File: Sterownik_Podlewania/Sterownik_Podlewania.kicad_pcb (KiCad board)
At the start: 2 copper layers, 89 parts, among them J1 Conn_01x06_Socket, J10 Screw_Terminal_01x02, J11 Screw_Terminal_01x02, J12 Screw_Terminal_01x02, J13 Screw_Terminal_01x02, J14 Screw_Terminal_01x02, J15 Screw_Terminal_01x02, J16 Screw_Terminal_01x02, J2 Conn_01x06_Socket, J3 RJ45, J4 Conn_01x04_Socket, J5 RJ45, J6 RJ45, J7 Conn_01x05_Socket, J8 RJ45, J9 Screw_Terminal_01x02, K1 SANYOU_SRD_Form_C, K2 SANYOU_SRD_Form_C, K3 SANYOU_SRD_Form_C, K4 SANYOU_SRD_Form_C, K5 SANYOU_SRD_Form_C, Q1 BC547, Q2 BC547, Q3 BC547, Q4 BC547, Q5 BC547, SW1 SW_Nidec_CAS-120A1, SW2 SW_Nidec_CAS-120A1, SW3 SW_Nidec_CAS-120A1, SW4 SW_Nidec_CAS-120A1, SW5 SW_Nidec_CAS-120A1, SW6 SW_Nidec_CAS-120A1, SW8 SW_Nidec_CAS-120A1, U1 ESP32-DEVKITC, U2 HHG1D-1, U3 L7805

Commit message: Dodanie footprintów schotky, kondesatorów
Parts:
- added C10: 0.1u, Capacitor_THT:C_Disc_D3.0mm_W1.6mm_P2.50mm, F.Cu at (487.2, 88.5)
- added C7: 0.33u, Capacitor_THT:CP_Axial_L10.0mm_D4.5mm_P15.00mm_Horizontal, F.Cu at (453.0, 86.7)
- added C8: 0.1u, Capacitor_THT:C_Disc_D3.0mm_W1.6mm_P2.50mm, F.Cu at (483.8, 75.0)
- added C9: 0.1u, Capacitor_THT:C_Disc_D3.0mm_W1.6mm_P2.50mm, F.Cu at (482.8, 81.5)
- added D19: D_Schottky, Diode_SMD:D_SOD-123, F.Cu at (-149.8, -12.7)
- added D20: D_Schottky, Diode_SMD:D_SOD-123, F.Cu at (-149.8, -9.34)
- added D21: D_Schottky, Diode_SMD:D_SOD-123, F.Cu at (-149.8, -3.99)
- added U4: LD1117S33TR_SOT223, Package_TO_SOT_SMD:SOT-223-3_TabPin2, F.Cu at (4.42, 3.70)
- J4: footprint Connector_Harwin:Harwin_M20-89006xx_1x06_P2.54mm_Horizontal -> Connector_Harwin:Harwin_M20-89004xx_1x04_P2.54mm_Horizontal

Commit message: Dodanie modeli 3d, nowy footprint do przełącznika, przerzucenie na drugą stronę płytki elementów, wstępne rozdzielenie elemntów pasywnych
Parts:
- C1, C11, C2, C3, C4, C5, C6, R11, R12, R14, R16, R18, R20, R21, R22, R23, R24, R25, R26, R27, R28, R3, R6, R7, R8, R9: moved to B.Cu
- J1, J2: footprint Connector_Harwin:Harwin_M20-89006xx_1x06_P2.54mm_Horizontal -> Connector_PinHeader_2.54mm:PinHeader_1x06_P2.54mm_Vertical
- J4: footprint Connector_Harwin:Harwin_M20-89004xx_1x04_P2.54mm_Horizontal -> Connector_PinHeader_2.54mm:PinHeader_1x04_P2.54mm_Vertical
- J7: footprint Connector_Harwin:Harwin_M20-89005xx_1x05_P2.54mm_Horizontal -> Connector_PinHeader_2.54mm:PinHeader_1x05_P2.54mm_Vertical
- SW1, SW2, SW3, SW4, SW5, SW6, SW8: footprint Button_Switch_SMD:Nidec_Copal_CAS-120A -> Toggle_Switch:Toggle Switch Bootland 4.7mm
- U1: footprint RF_Module:ESP32-C3-DevKitM-1 -> ESP32:MODULE_ESP32-DEVKITC
- U2: footprint Relay_THT:Relay_NCR_HHG1D-1 -> Relay_THT:RELAY_G3MB-202P
- U4: footprint Package_TO_SOT_SMD:SOT-223-3_TabPin2 -> Package_TO_SOT_THT:TO-220-3_Vertical
- moved C3 469.6 mm to (63.8, 157.7), turned to 90 degrees
- moved R24 464.2 mm to (70.3, 165.6), turned to 180 degrees
- moved R14 452.2 mm to (70.0, 144.8), turned to 180 degrees
- moved R17 434.7 mm to (86.6, 116.8)
- moved C2 434.1 mm to (97.8, 156.4), turned to 90 degrees
- moved R19 433.0 mm to (79.4, 116.6)
- moved R13 431.8 mm to (84.0, 121.9)
- moved R23 425.5 mm to (105.3, 167.1), turned to 180 degrees
- moved C11 424.7 mm to (113.3, 157.5), turned to 90 degrees
- moved C4 422.3 mm to (88.2, 151.1), turned to 180 degrees
- moved R16 420.4 mm to (85.5, 141.0), turned to 180 degrees
- moved R15 420.4 mm to (90.1, 122.2)
- moved R28 420.2 mm to (119.3, 165.6), turned to 180 degrees
- moved R25 417.2 mm to (92.6, 147.8), turned to 180 degrees
- moved D12 416.4 mm to (75.8, 69.3)
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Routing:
- net (no net): vias 0 -> 6

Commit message: dodanie modeli 3d, poprawa footprintu RTC
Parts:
- removed J2: Conn_01x06_Socket, Connector_PinHeader_2.54mm:PinHeader_1x06_P2.54mm_Vertical
- removed J7: Conn_01x05_Socket, Connector_PinHeader_2.54mm:PinHeader_1x05_P2.54mm_Vertical
- added J18: RJ45, Connector_RJ:RJ45_Amphenol_54602-x08_Horizontal, F.Cu at (41.9, 71.1)
- added R29: R, Resistor_SMD:R_1206_3216Metric, B.Cu at (153.9, 76.2)
- added R30: R, Resistor_SMD:R_1206_3216Metric, B.Cu at (153.9, 79.5)
- added U5: 757, Voltage_Level_Converters:MODULE_757, F.Cu at (81.3, 113.0)
- added U6: ~, RTC:RTC DS1307 + 32kb EEPROM 24C32 I2C, F.Cu at (113.7, 115.6)
- C7: footprint Capacitor_THT:CP_Axial_L10.0mm_D4.5mm_P15.00mm_Horizontal -> Capacitor_SMD:CP_Elec_4x5.4
- D10, D14, D16, D8, R1, R10, R13, R15, R17, R19, R2, R4, R5: moved to B.Cu
- J1: value Conn_01x06_Socket -> Barrel_Jack_MountingPin; footprint Connector_PinHeader_2.54mm:PinHeader_1x06_P2.54mm_Vertical -> Connector_BarrelJack:BarrelJack_GCT_DCJ200-10-A_Horizontal
- moved R22 115.1 mm to (77.2, 122.4)
- moved R3 115.1 mm to (82.3, 98.2)
- moved R6 115.1 mm to (82.9, 103.1)
- moved R7 115.1 mm to (101.4, 111.5)
- moved R8 115.1 mm to (102.8, 119.6)
- moved R9 115.1 mm to (92.4, 127.5)
- moved C8 113.6 mm to (66.0, 96.5)
- moved C9 102.5 mm to (76.2, 96.5)
- moved C10 102.4 mm to (86.4, 96.5)
- moved D21 98.0 mm to (98.2, 96.5)
- moved C7 97.2 mm to (58.5, 81.5), turned to 0 degrees
- moved R15 97.0 mm to (45.4, 36.1), turned to 180 degrees
- moved R10 96.0 mm to (46.6, 24.9), turned to 180 degrees
- moved R17 94.0 mm to (49.0, 30.7), turned to 180 degrees
- moved J1 92.6 mm to (43.5, 56.2), turned to -90 degrees
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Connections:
- J1 pad 1: SDA -> VP
- J1 pad 2: SCL -> GND
- U1 pad 4: unconnected-(U1-SENSOR_VN-Pad4) -> /Czujnik ciśnienia output
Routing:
- net (no net): vias 6 -> 3

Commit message: Wstępny finalny rozkład płytki, narysowanie outlinu
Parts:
- added REF**: MountingHole_3.2mm_M3_Pad_Via, MountingHole:MountingHole_3.2mm_M3_Pad_Via, F.Cu at (197.5, 150.0)
- added REF**: MountingHole_3.2mm_M3_Pad_Via, MountingHole:MountingHole_3.2mm_M3_Pad_Via, F.Cu at (42.5, 40.0)
- added REF**: MountingHole_3.2mm_M3_Pad_Via, MountingHole:MountingHole_3.2mm_M3_Pad_Via, F.Cu at (42.5, 150.0)
- added REF**: MountingHole_3.2mm_M3_Pad_Via, MountingHole:MountingHole_3.2mm_M3_Pad_Via, F.Cu at (197.5, 40.0)
- D12: moved to B.Cu
- R1, R2: moved to F.Cu
- U4: footprint Package_TO_SOT_THT:TO-220-3_Vertical -> Package_TO_SOT_SMD:SOT-223
- moved R5 166.1 mm to (193.5, 97.5)
- moved R4 164.3 mm to (193.2, 89.8)
- moved R2 143.9 mm to (152.5, 105.0), turned to 0 degrees
- moved J1 139.9 mm to (183.2, 48.6), turned to 180 degrees
- moved R1 135.8 mm to (152.5, 100.5)
- moved C7 129.0 mm to (187.5, 79.3), turned to 90 degrees
- moved R10 113.1 mm to (118.4, 112.2), turned to 90 degrees
- moved C8 112.2 mm to (174.2, 67.0)
- moved R22 106.6 mm to (182.7, 137.2)
- moved D2 103.8 mm to (193.9, 95.0)
- moved R3 100.7 mm to (182.6, 89.7)
- moved R6 99.8 mm to (182.6, 99.7)
- moved R19 99.2 mm to (129.1, 97.7), turned to 90 degrees
- moved J8 98.9 mm to (49.0, 51.0)
- moved C9 97.6 mm to (167.0, 60.8), turned to -90 degrees
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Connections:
- U1 pad 15: /WIFI -> /SEN0193_WYJŚCIE
- U1 pad 23: /SEN0193_WYJŚCIE -> /TRYB
- U1 pad 24: /TRYB -> /WIFI
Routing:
- net (no net): track 0.00 -> 160.0 mm
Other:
- board outline added: 165 x 120 mm

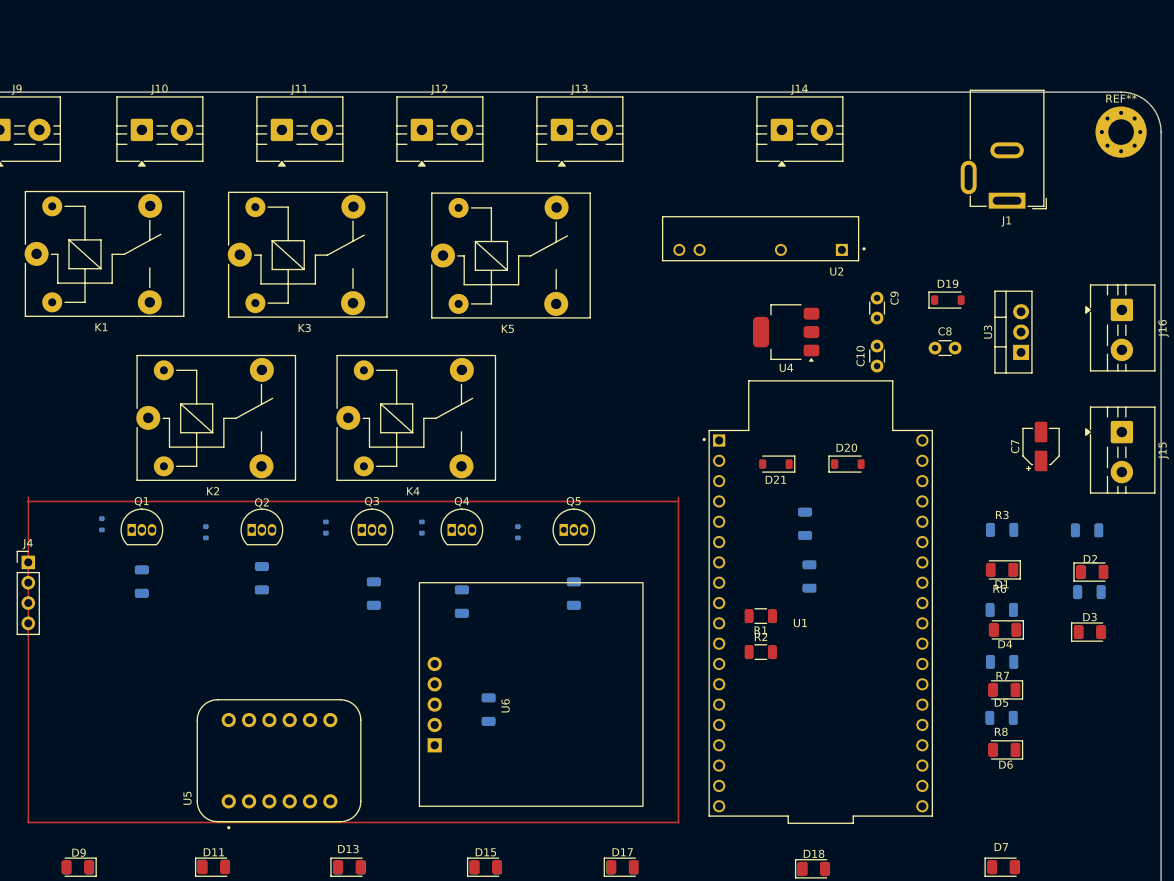
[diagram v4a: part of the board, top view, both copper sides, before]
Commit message: Zmiana footprintó diód przekaźnika na schottky,finalne ułożenie  przekaźników, diód itp
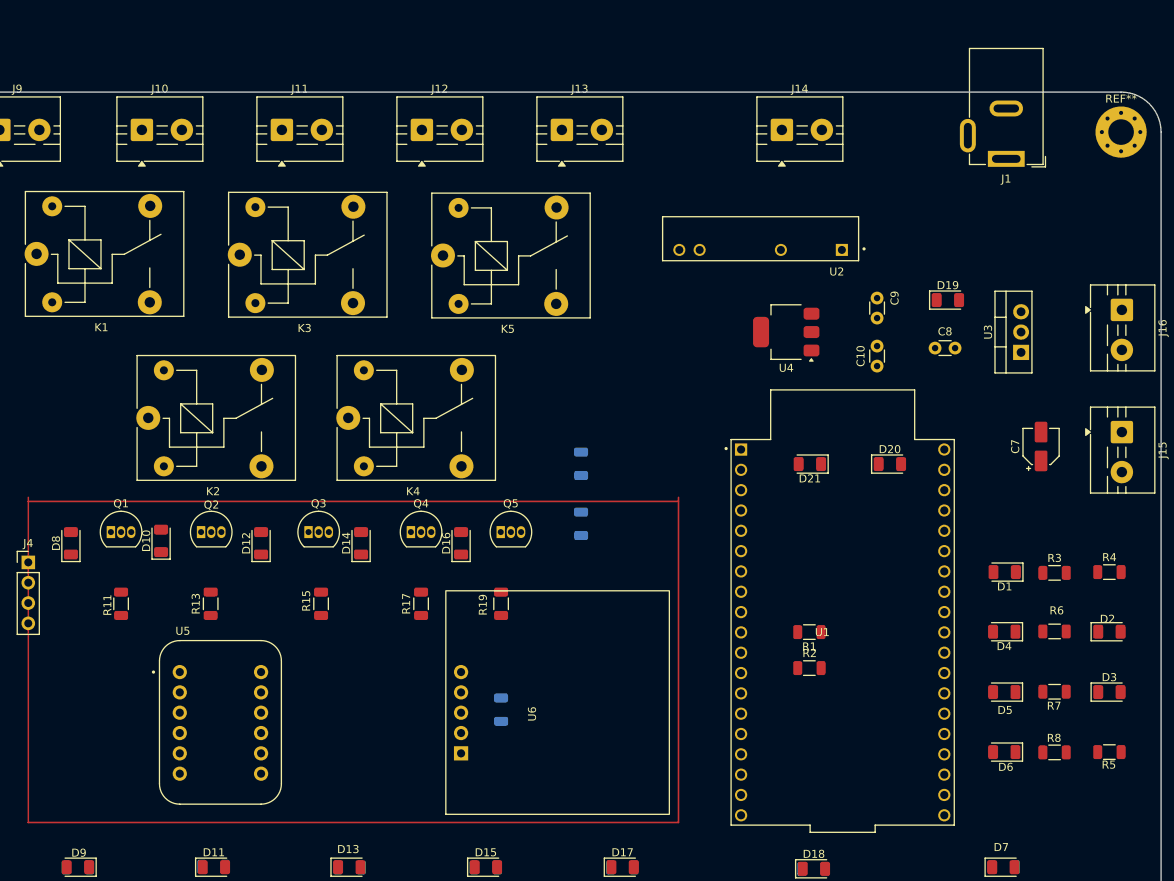
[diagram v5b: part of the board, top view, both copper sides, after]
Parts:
- D10, D12, D14, D16, D8: footprint Diode_SMD:D_SOD-523 -> Diode_SMD:D_1206_3216Metric; moved to F.Cu
- D19, D20, D21: footprint Diode_SMD:D_SOD-123 -> Diode_SMD:D_1206_3216Metric
- R11, R13, R15, R17, R19, R3, R4, R5, R6, R7, R8: moved to F.Cu
- moved R30 31.8 mm to (130.0, 81.5)
- moved R29 28.0 mm to (130.0, 89.0)
- moved R5 20.2 mm to (196.0, 117.5)
- moved R19 9.19 mm to (120.0, 99.0)
- moved U5 8.76 mm to (84.9, 113.8), turned to 0 degrees
- moved R3 8.47 mm to (189.2, 95.1), turned to 0 degrees
- moved D12 8.34 mm to (90.0, 91.4)
- moved R8 7.90 mm to (189.2, 117.5)
- moved D3 7.89 mm to (196.0, 110.0)
- moved Q5 7.87 mm to (120.0, 90.0)
- moved D14 7.85 mm to (102.5, 91.4), turned to 90 degrees
- moved D2 7.76 mm to (196.0, 102.5)
- moved R7 7.54 mm to (189.2, 110.0), turned to 180 degrees
- moved D16 7.23 mm to (115.0, 91.4)
- moved R13 7.15 mm to (83.7, 99.0)
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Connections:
- net /Sekcja 1_5V renamed /Pompa_230_5V
- C11 pad 1: /Sekcja 1 M -> /Pompa_230 M
- C2 pad 1: /Sekcja 6 M -> /Sekcja 1 M
- D9 pad 2: /Sekcja 6 -> /Sekcja 1
- R11 pad 1: /Sekcja 6 -> /Sekcja 1
- SW2 pad 2: /Sekcja 6 M -> /Sekcja 1 M
- SW8 pad 2: /Sekcja 1 M -> /Pompa_230 M
- U1 pad 13: /Sekcja 6 -> /Pompa_230 M
- U1 pad 15: /SEN0193_WYJŚCIE -> /Pompa_230
- U1 pad 28: /Sekcja 3 -> /Sekcja 2 M
- U1 pad 29: /Sekcja 4 -> /Sekcja 2
- U1 pad 33: /Sekcja 6 M -> /SEN0193_WYJŚCIE
- U1 pad 36: /Sekcja 5 M -> /Sekcja 1 M
- U1 pad 37: /Sekcja 4 M -> /Sekcja 1
- U1 pad 5: /Sekcja 1 M -> /Sekcja 3 M
- U1 pad 6: /Sekcja 2 M -> /Sekcja 3
- U1 pad 7: /Sekcja 3 M -> /Sekcja 4 M
- U1 pad 8: /Sekcja 1 -> /Sekcja 4
- U1 pad 9: /Sekcja 2 -> /Sekcja 5 M
- U5 pad A3: /Sekcja 1 -> /Pompa_230
